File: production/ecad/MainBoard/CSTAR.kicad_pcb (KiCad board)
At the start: 4 copper layers, 152.4 x 152.4 mm, 180 parts, among them IC1 LT8648SEV#PBF, J1 Conn_01x02_Pin, J10 Conn_01x03_Pin, J11 B4B-PH-K-S, J12 B4B-PH-K-S, J13 Conn_01x03_Pin, J13 Conn_01x05_Pin, J14 Conn_01x03_Pin, J15 Conn_01x03_Pin, J16 Conn_01x03_Pin, J17 Ultra_4, J18 Ultra_3, J19 Ultra_2, J2 Conn_01x02_Pin, J20 RX connect, J21 Ultra_1, J22 TX connect, J23 Conn_01x02_Pin, J24 Conn_01x02_Pin, J25 TYPE-C-31-M-12, J26 532610771, J28 532610771, J29 Conn_01x04_Socket, J3 Conn_01x02_Pin, J30 691137710002, J31 TYPE-C-31-M-12, J4 XT60PW-M, J5 Conn_01x02_Pin, J6 Conn_01x02_Pin, J7 532610771, J8 Conn_01x03_Pin, J9 Conn_01x03_Pin, Q1 AO3400A, Q2 AO3400A, Q3 AO3400A, Q4 AO3400A, Q5 AO3400A, Q6 AO3400A, Q7 AO3400A, Q8 IRFHM9331TRPBF, SW1 SW_Push, SW2 SW_Push, SW3 SW_Push, SW4 SW_Push, U1 AZ1117IH-3.3TRG1, U2 DRV8842PWPR, U3 DRV8842PWPR, U4 TXB0104DR, U5 CP2102N-A01-GQFN28, U6 ESP32-WROOM-32UE_M113EH6400UH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, U7 TXB0104DR, U8 CP2102N-A01-GQFN28, U9 ESP32-WROOM-32UE_M113EH6400UH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, X1 B2P-VH, X2 B2P-VH

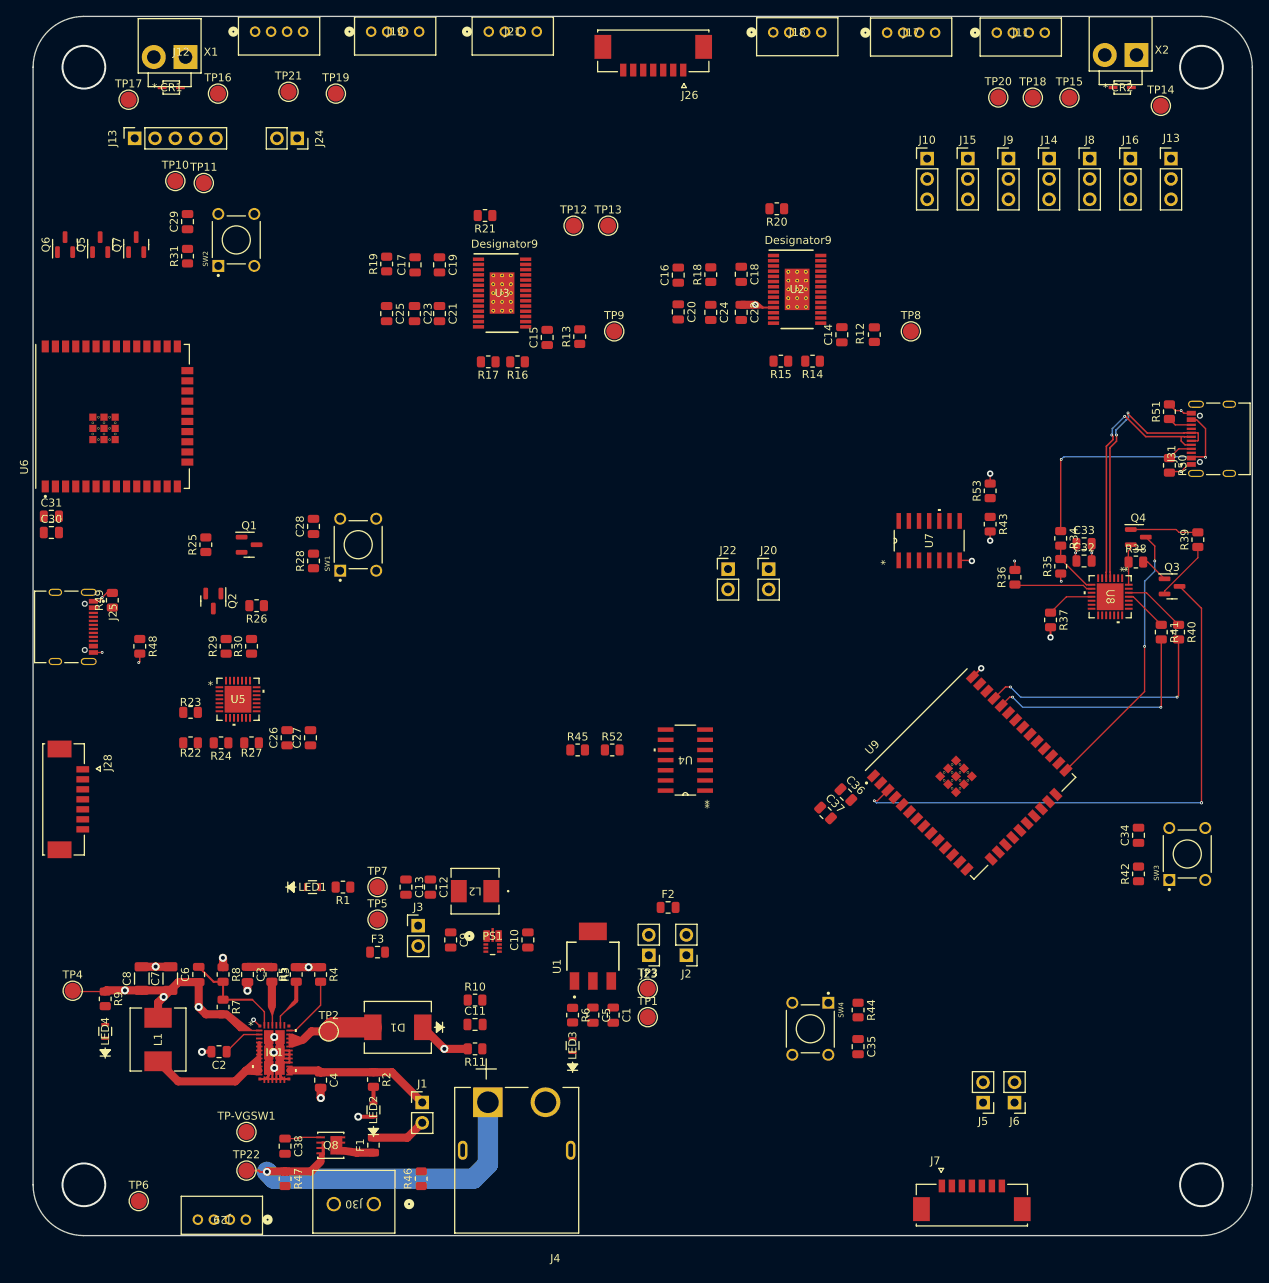
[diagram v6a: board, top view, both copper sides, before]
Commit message: resetting before to restore my work (sorry Vasishta, pull next time)
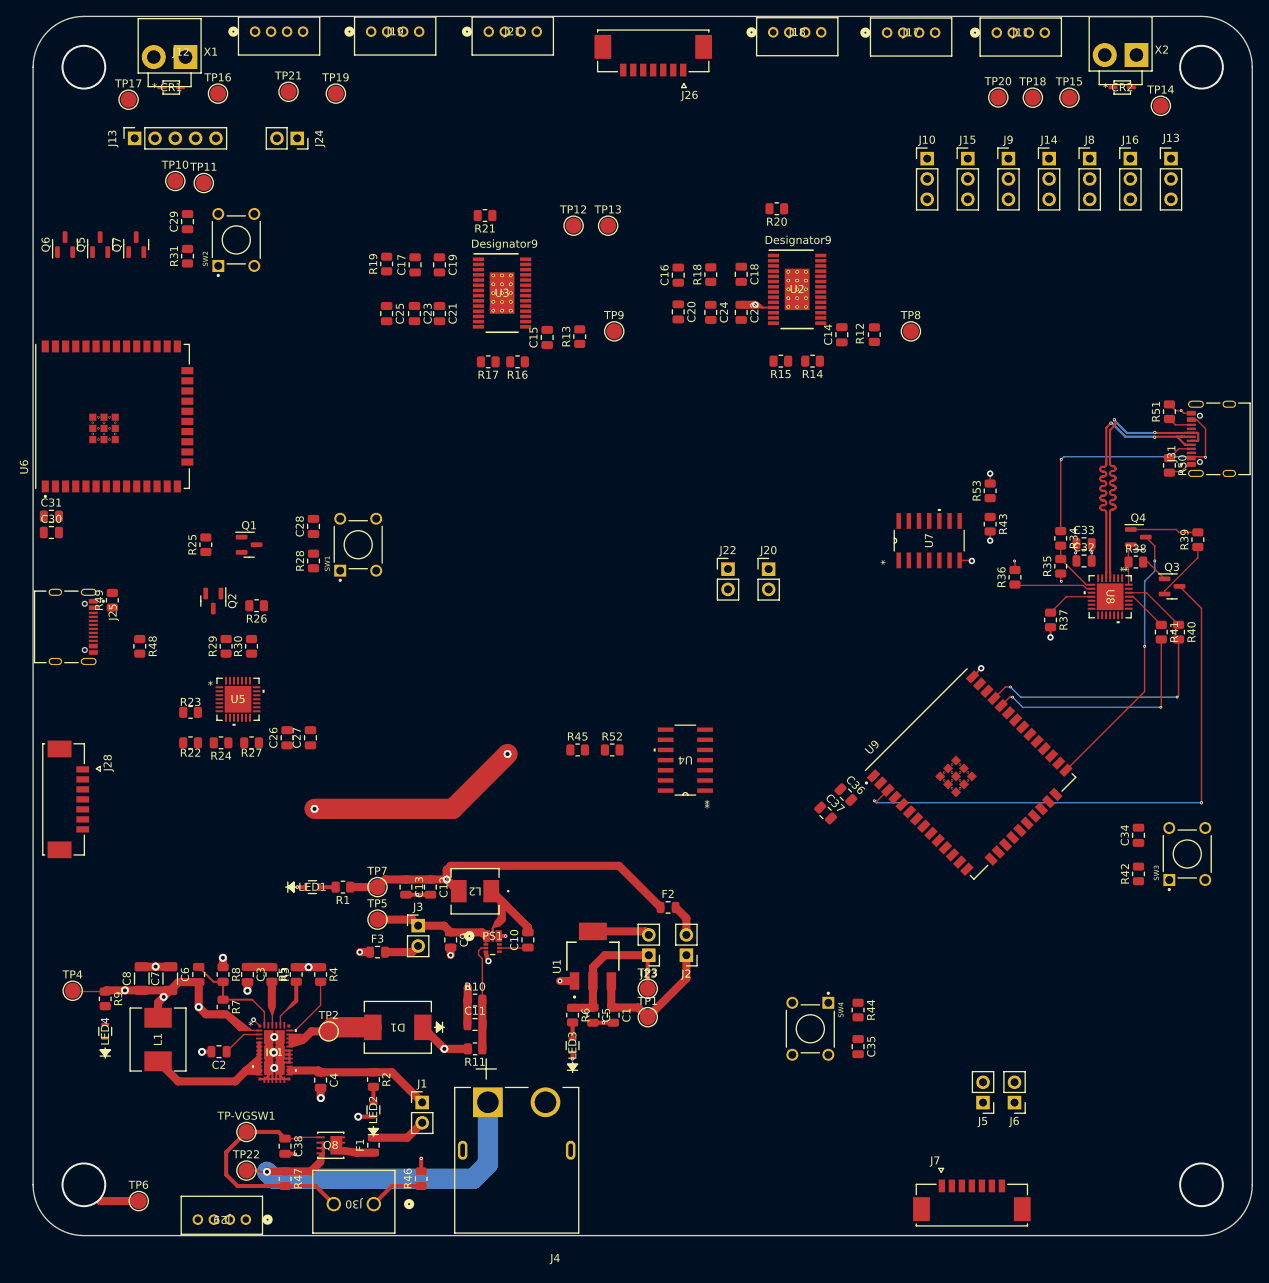
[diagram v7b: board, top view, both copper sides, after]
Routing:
- net +5V: track 0.00 -> 49.5 mm, vias 0 -> 2
- net (no net): track 0.00 -> 27.1 mm, vias 4 -> 2
- net Net-(C38-Pad1): track 4.51 -> 31.1 mm
- net +3V3: track 3.31 -> 22.8 mm
- net Net-(J2-Pin_1): track 0.00 -> 18.0 mm
- net GND: track 77.2 -> 95.0 mm, vias 23 -> 34
- net Net-(J3-Pin_1): track 0.00 -> 15.5 mm
- net Net-(PS1-FB): track 0.00 -> 13.5 mm
- net Net-(PS1-SW): track 0.00 -> 13.0 mm
- net Net-(J23-Pin_2): track 0.00 -> 7.17 mm
- net Net-(J30-Pad1): track 0.00 -> 6.86 mm
- net USB2_D-: track 33.2 -> 38.9 mm
- net Net-(J3-Pin_2): track 0.00 -> 4.46 mm
- net Net-(J2-Pin_2): track 0.00 -> 3.99 mm
- net USB2_D+: track 33.9 -> 37.9 mm
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- added copper zone on In2.Cu, net +3V3
- added copper zone on In2.Cu, net +5V

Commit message: diff pair and minor changes
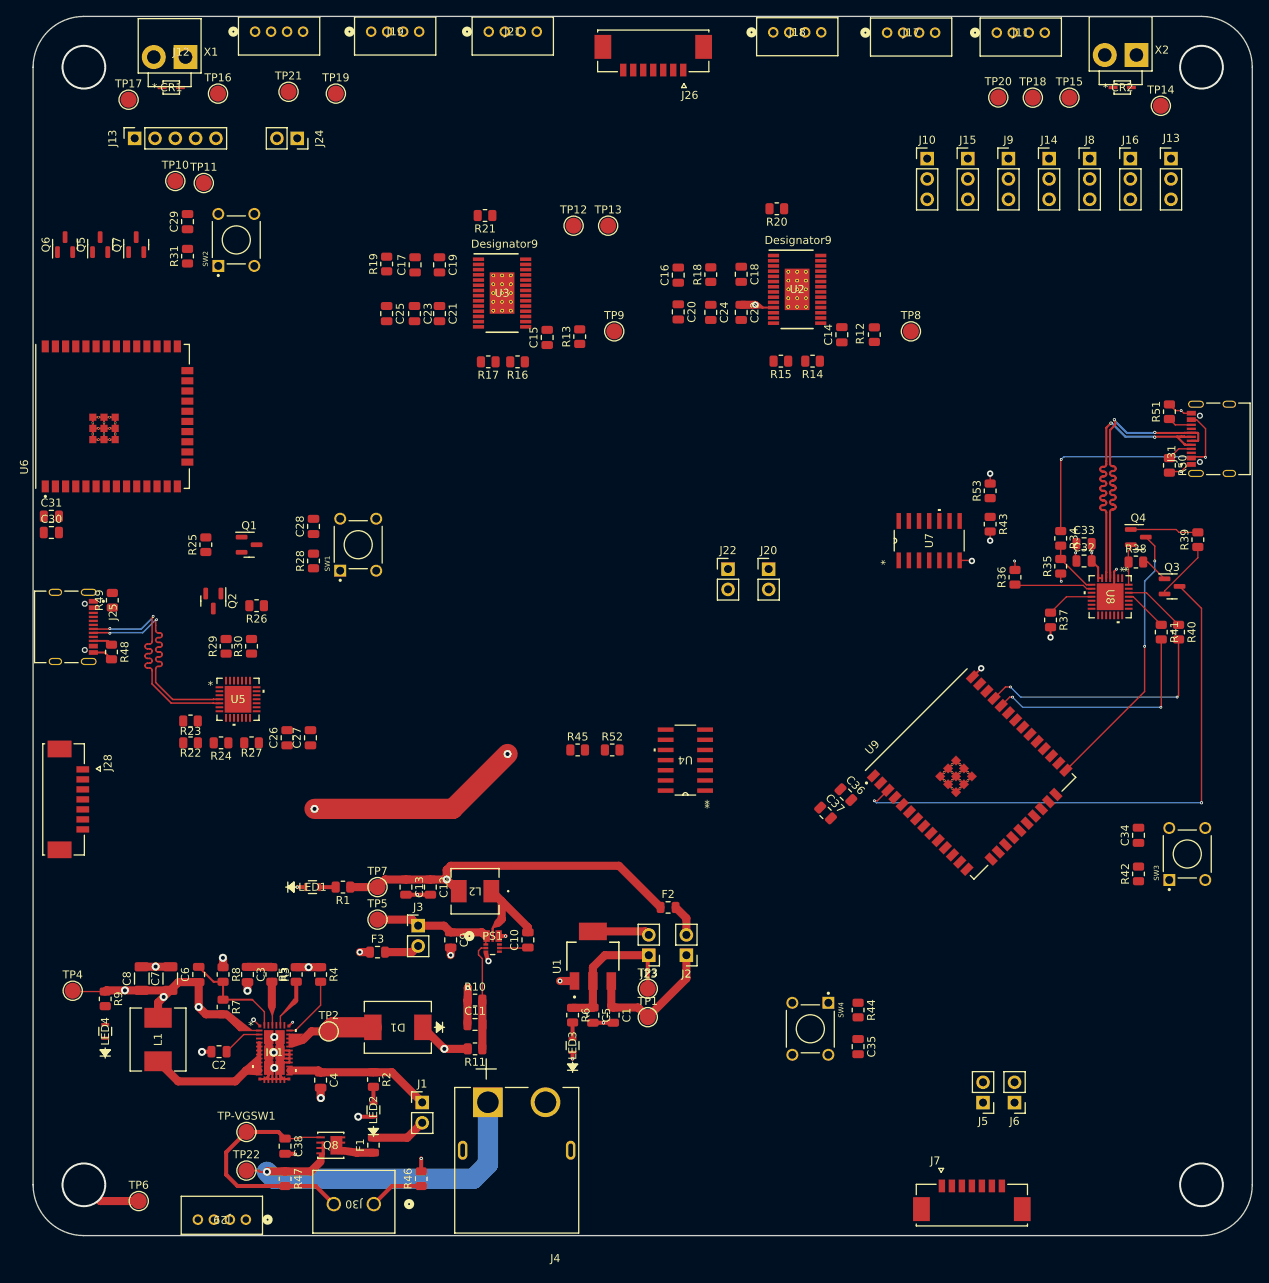
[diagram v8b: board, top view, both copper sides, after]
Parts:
- moved R48 3.61 mm to (60.6, 130.2)
- moved R23 1.08 mm to (70.5, 138.9), turned to 0 degrees
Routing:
- net GND: track 95.0 -> 135.7 mm, vias 34 -> 36
- net USB1_D-: track 0.00 -> 29.8 mm, vias 0 -> 2
- net USB1_D+: track 0.00 -> 29.7 mm, vias 0 -> 2
- net +3V3: track 22.8 -> 25.7 mm
- net Net-(J25-CC2): track 0.00 -> 2.46 mm
- net Net-(IC1-SYNC/MODE): track 4.85 -> 6.29 mm
